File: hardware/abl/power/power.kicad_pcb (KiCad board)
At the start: 2 copper layers, 110 x 75.9 mm, 39 parts, among them J1 Screw_Terminal_01x03, J2 Screw_Terminal_01x03, J3 009159008603906, U1 TWGMC AMS1117-3.3, U2 TMP1075D, U3 INA219AxD

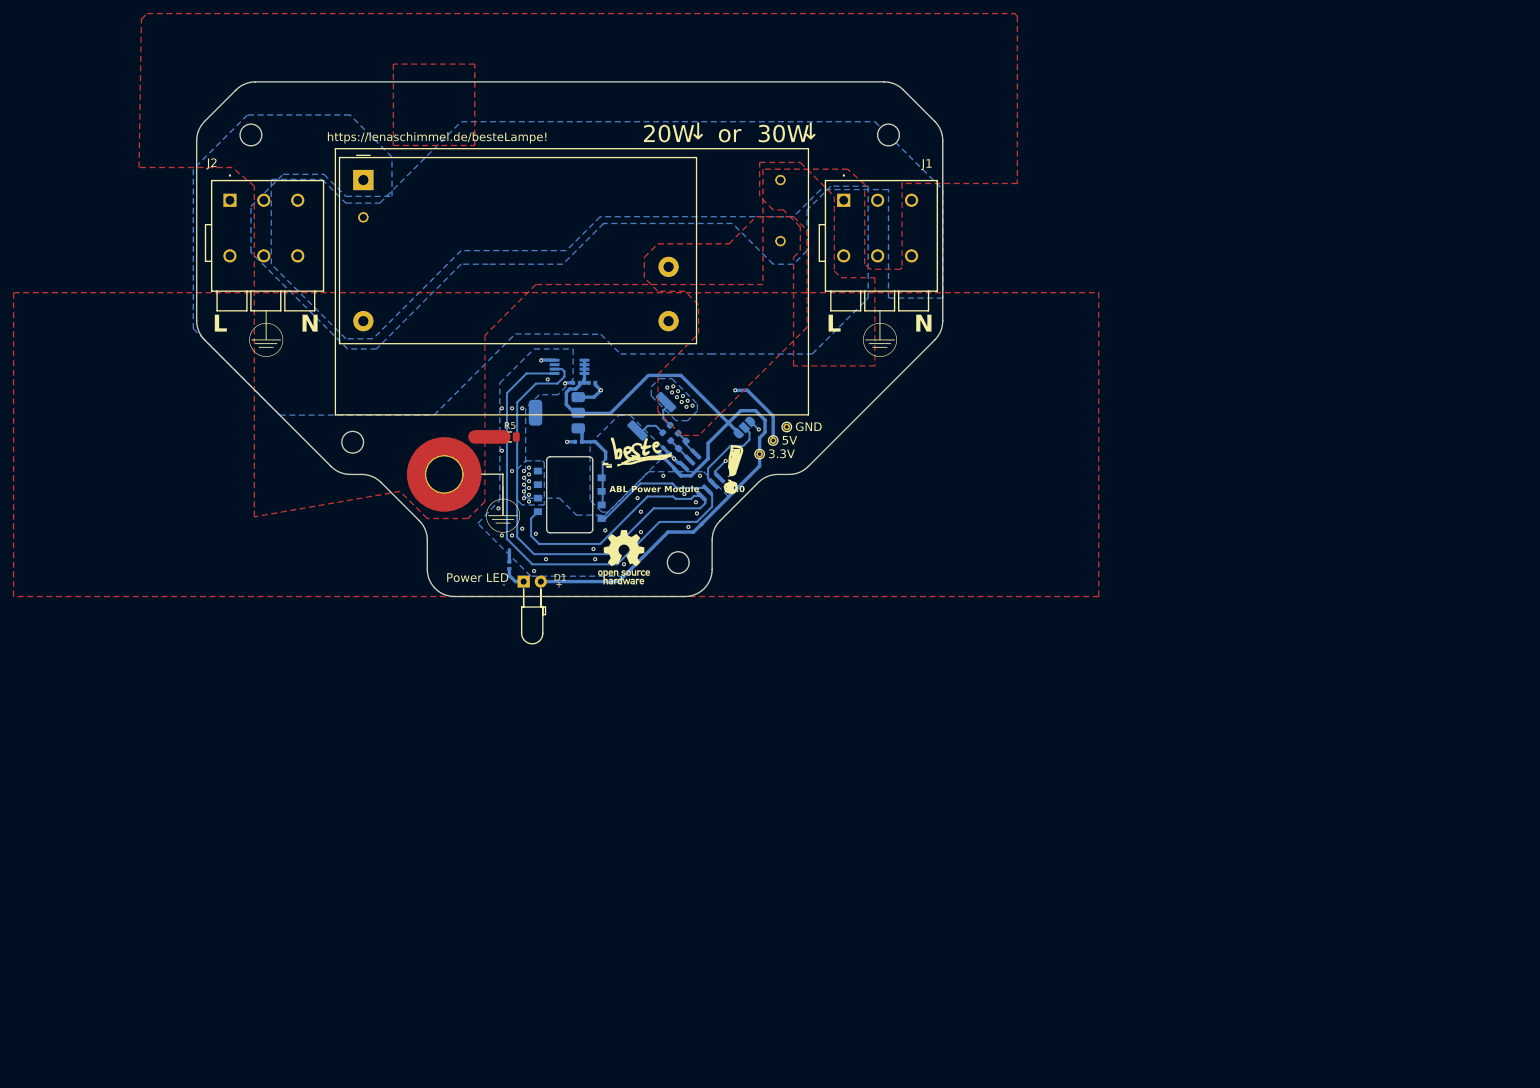
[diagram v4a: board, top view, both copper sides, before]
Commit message: More minor optimizatios, add meta data.
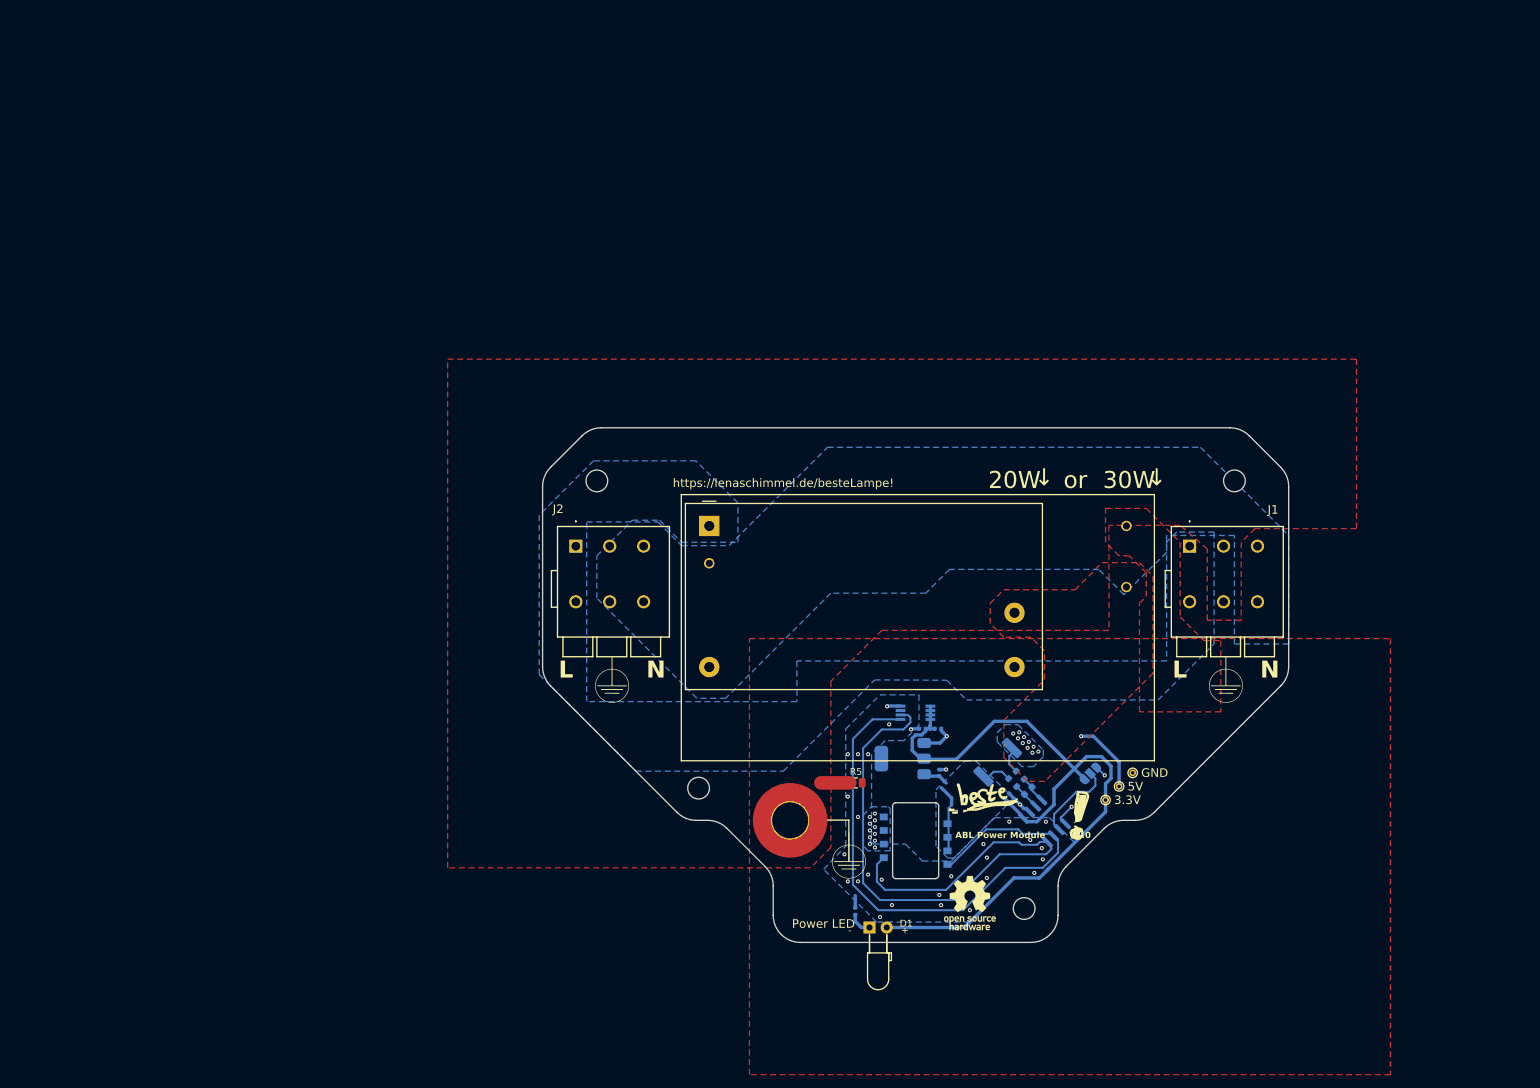
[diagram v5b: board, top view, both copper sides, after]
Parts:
- moved C1 72.2 mm to (153.5, 90.0), turned to 90 degrees
- moved C2 72.1 mm to (153.3, 83.5)
- moved G*** 72.1 mm to (140.2, 102.2)
- moved C3 72.1 mm to (151.0, 83.5)
- moved C4 72.1 mm to (164.3, 94.3)
- moved C5 72.1 mm to (163.4, 93.4)
- moved C6 72.1 mm to (166.6, 92.6)
- moved D1 72.1 mm to (143.2, 112.8)
- moved G*** 72.1 mm to (165.4, 95.6)
- moved G*** 72.1 mm to (195.8, 76.2)
- moved G*** 72.1 mm to (105.2, 76.2)
- moved G*** 72.1 mm to (105.2, 71.0)
- moved G*** 72.1 mm to (133.8, 107.1)
- moved G*** 72.1 mm to (195.8, 71.0)
- moved H1 72.1 mm to (103.0, 47.0)
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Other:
- outline, holes or cut-outs redrawn
- board text added: "Always bridge 2 pads to indicate PS wattage:"
- board text removed: "+5V"
- board text removed: "Always bridge 2 pads to indicate wattage:"

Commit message: Implemented proposed changes.
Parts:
- added C7: 33uF, Capacitor_Tantalum_SMD:CP_EIA-3528-21_Kemet-B, B.Cu at (158.1, 81.5)
- C1: value 10u -> 33uF; footprint Capacitor_SMD:C_0402_1005Metric -> Capacitor_Tantalum_SMD:CP_EIA-3528-21_Kemet-B
- J1, J2: value Screw_Terminal_01x03 -> Terminal_01x03
- moved C2 8.29 mm to (145.1, 84.7), turned to 0 degrees
- moved U2 6.58 mm to (143.4, 80.9)
- moved U1 6.32 mm to (151.7, 82.7)
- moved C3 5.90 mm to (145.1, 83.5)
- moved R5 3.45 mm to (137.9, 90.5)
- moved C1 1.98 mm to (154.8, 88.5), turned to 180 degrees
- moved REF** 1.10 mm to (118.5, 66.2)
- moved G*** 0.36 mm to (195.4, 71.0)
- moved G*** 0.35 mm to (104.9, 71.0)
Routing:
- net GND: track 19.8 -> 9.09 mm, vias 44 -> 63
- net /5VMSR: track 17.4 -> 10.5 mm
- net /SCL: track 96.8 -> 91.9 mm
- net /SDA: track 85.8 -> 81.1 mm
- net Earth_Protective: track 4.27 -> 0.00 mm
- net +3.3V: track 110.6 -> 109.7 mm

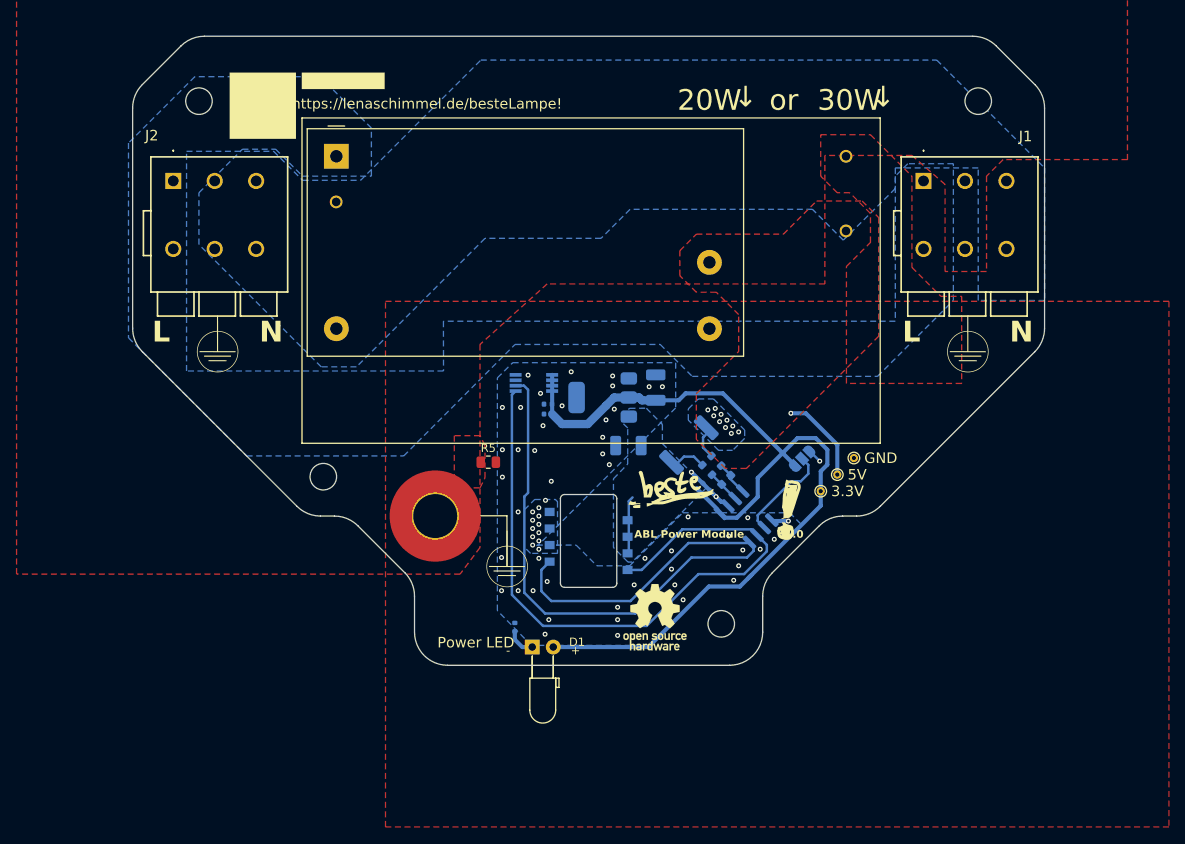
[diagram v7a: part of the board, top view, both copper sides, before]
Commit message: Add own / optimized footprints (bigger pads), add fuse and current limiting to the power module.
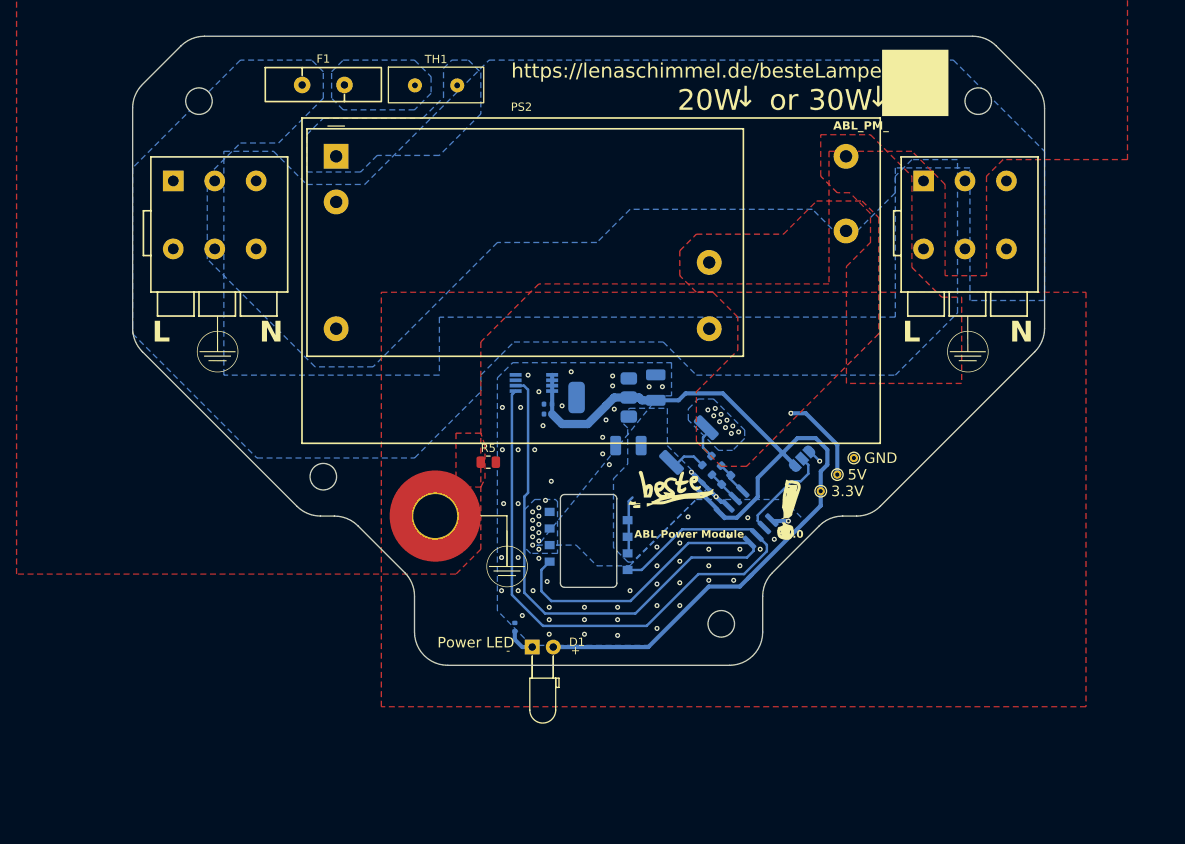
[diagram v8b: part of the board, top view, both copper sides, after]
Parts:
- removed PS1: IRM-20-5, Converter_ACDC:Converter_ACDC_MeanWell_IRM-20-xx_THT
- removed REF**: OSHW-Logo_7.5x8mm_SilkScreen, Symbol:OSHW-Logo_7.5x8mm_SilkScreen
- removed REF** (x2): Symbol_HighVoltage_Triangle_6x6mm_Copper, Symbol:Symbol_HighVoltage_Triangle_6x6mm_Copper
- added F1: MF-RM040-240, Own footprints:Bourns MF-RM055-240 resettable fuse, F.Cu at (118.0, 45.0)
- added TH1: CL-140, Own footprints:Amphenol NTC Inrush Current Limiter CL-140, F.Cu at (131.6, 45.0)
- J1, J2: footprint WAGO-2604-1103:26041103 -> Own footprints:WAGO-2604-1103
- PS2: footprint IRM-30:IRM-30_MWU -> Own footprints:Converter_ACDC_MeanWell_IRM-20+30-xx_THT_combined
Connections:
- PS2 pad 1: /L -> Net-(PS2-AC/L)
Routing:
- net GND: vias 63 -> 76
- added copper zone on B.Cu, net Net-(F1-Pad2)
- added copper zone on B.Cu, net Net-(PS2-AC/L)
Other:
- board text added: "ABL_PM_"
